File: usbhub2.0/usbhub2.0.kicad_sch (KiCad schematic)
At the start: 31 parts, among them J1 Conn_01x05_Male, J2 Conn_01x05_Male, J4 Conn_01x05_Male, J5 USB_InputPort, J7 Conn_01x05_Male, J9 Power, U1 FE1.1s, Y1 Crystal_12MHz

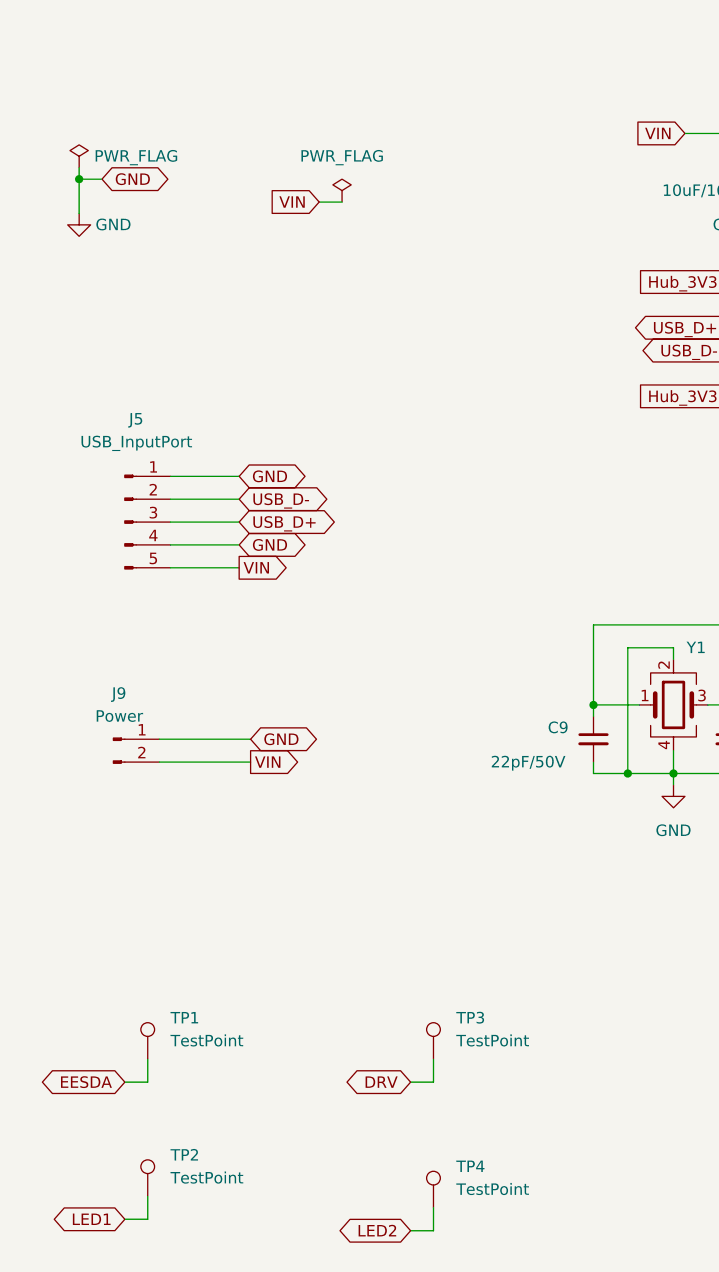
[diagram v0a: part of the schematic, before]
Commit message: change usbhub2.0 board design
* remove usb molex input and add usb-c to input channel
* change usbout1 molex to pin header
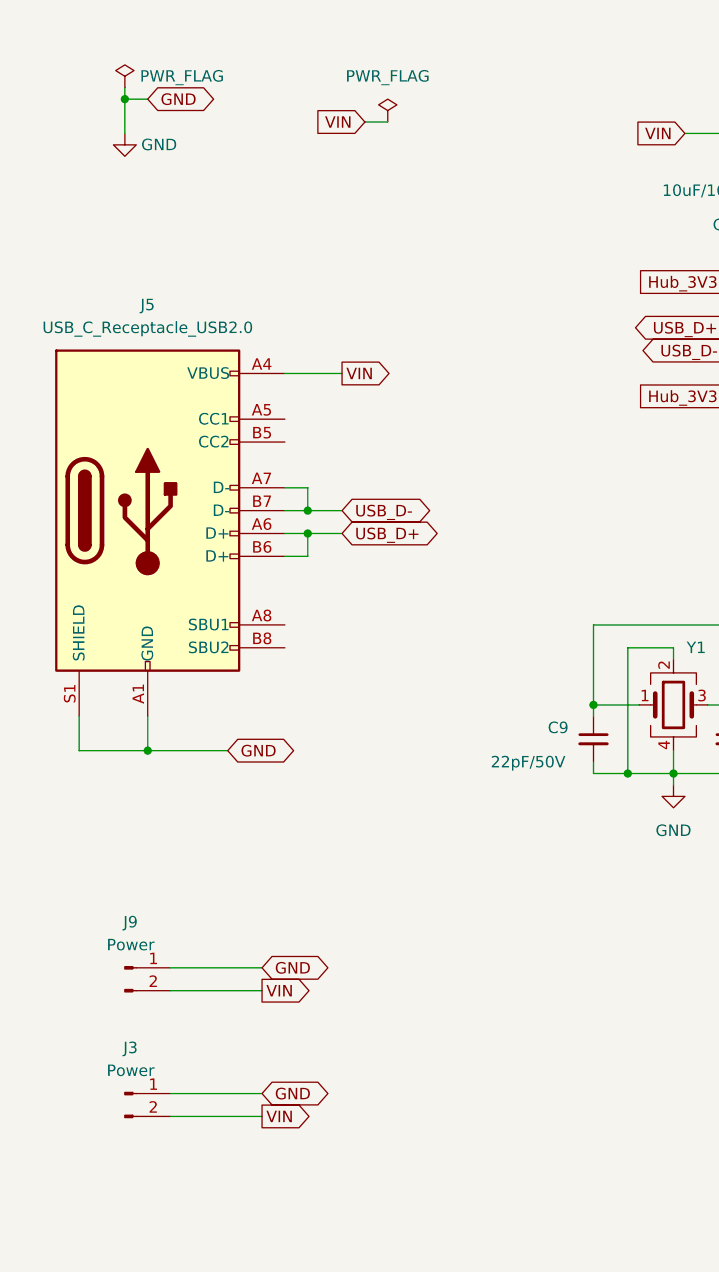
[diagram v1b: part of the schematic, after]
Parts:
- removed J5: USB_InputPort, Connector_Molex:Molex_PicoBlade_53261-0571_1x05-1MP_P1.25mm_Horizontal, symbol Connector:Conn_01x05_Male
- removed TP1, TP2, TP3, TP4: TestPoint, TestPoint:TestPoint_Pad_D1.0mm, symbol Connector:TestPoint
- added J3: Power, Connector_PinHeader_2.54mm:PinHeader_1x02_P2.54mm_Vertical, symbol Connector:Conn_01x02_Male
- added J5: USB_C_Receptacle_USB2.0, Connector_USB:USB_C_Receptacle_HRO_TYPE-C-31-M-12, symbol Connector:USB_C_Receptacle_USB2.0
- J1: footprint Connector_Molex:Molex_PicoBlade_53261-0571_1x05-1MP_P1.25mm_Horizontal -> Connector_PinHeader_2.00mm:PinHeader_1x05_P2.00mm_Vertical
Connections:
- net GND: now also J3.1 (Pin_1), J5.A1 (GND), J5.A12 (GND), J5.B1 (GND), J5.B12 (GND), J5.S1 (SHIELD)
- net USB_D+: now also J5.A6 (D+), J5.B6 (D+)
- net USB_D-: now also J5.A7 (D-), J5.B7 (D-)
- net VIN: now also J3.2 (Pin_2), J5.A4 (VBUS), J5.A9 (VBUS), J5.B4 (VBUS), J5.B9 (VBUS)
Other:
- moved on the sheet: J9
